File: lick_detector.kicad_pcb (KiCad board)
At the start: 2 copper layers, 20 x 20 mm, 16 parts, among them P1 CONN_FFC_8_VERT, P2 RECEPTACLE_2MM, U1 ADXL313, U2 BUFFER_TRI_STATE, U3 BUFFER_2_ELEMENT

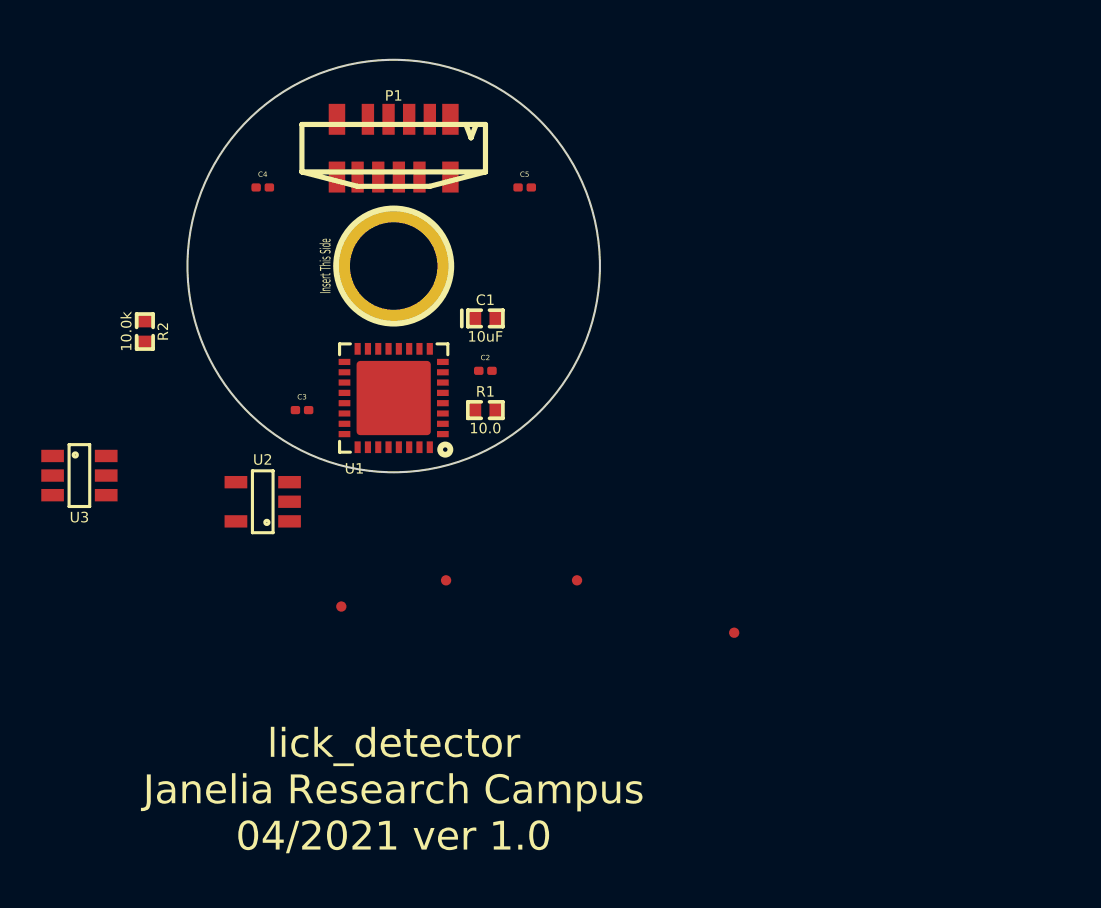
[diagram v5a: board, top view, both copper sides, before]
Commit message: Rearrange pcb footprints
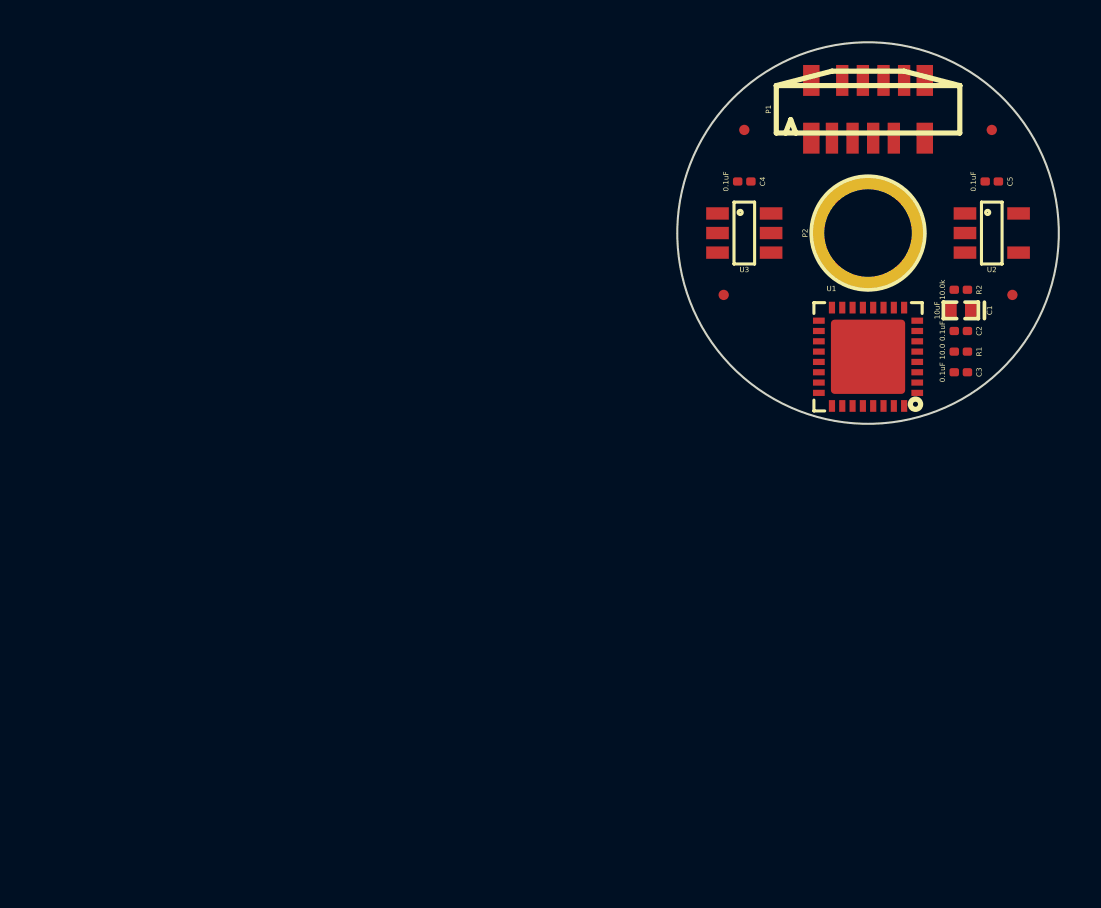
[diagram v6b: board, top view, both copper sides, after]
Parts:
- C2, C3, C4, C5: footprint lick_detector:C_0201_0603Metric -> lick_detector:SM0201
- R1, R2: footprint lick_detector:SM0402 -> lick_detector:SM0201
- moved R2 39.6 mm to (154.5, 102.8), turned to 180 degrees
- moved U2 37.7 mm to (156.0, 100.0), turned to 0 degrees
- moved U3 34.3 mm to (144.0, 100.0)
- moved C3 32.0 mm to (154.5, 106.8), turned to 180 degrees
- moved FID2 27.4 mm to (156.0, 95.0)
- moved FID1 26.2 mm to (144.0, 95.0)
- moved FID3 25.2 mm to (157.0, 103.0)
- moved FID4 23.9 mm to (143.0, 103.0)
- moved C4 23.4 mm to (144.0, 97.5), turned to 180 degrees
- moved R1 23.2 mm to (154.5, 105.8), turned to 180 degrees
- moved C2 23.1 mm to (154.5, 104.8), turned to 180 degrees
- moved U1 23.1 mm to (150.0, 106.0)
- moved P1 23.1 mm to (150.0, 94.0), turned to 0 degrees
- moved C1 23.1 mm to (154.5, 103.8), turned to 270 degrees
- moved P2 23.1 mm to (150.0, 100.0)
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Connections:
- R1 pad 1: Net-(R1-Pad1) -> VAA
- R1 pad 2: VAA -> Net-(R1-Pad2)
- U1 pad 5: Net-(R1-Pad1) -> Net-(R1-Pad2)
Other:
- board size 20 x 20 mm -> 18.5 x 18.5 mm

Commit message: Layout experimentation
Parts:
- U2: value BUFFER_TRI_STATE -> BUFFER_TRI_STATE_SMALL; footprint lick_detector:SOT-23-5 -> lick_detector:MICROPAK2_6LEAD
- U3: value BUFFER_2_ELEMENT -> BUFFER_2_ELEMENT_SMALL; footprint lick_detector:SOT-23-6 -> lick_detector:SOT-563
- moved FID3 3.35 mm to (158.5, 100.0)
- moved FID4 3.16 mm to (144.0, 106.0)
- moved C4 1.00 mm to (144.0, 98.5)
- moved C5 1.00 mm to (156.0, 98.5)
- moved FID1 1.00 mm to (144.0, 94.0)
- moved FID2 1.00 mm to (156.0, 94.0)
- moved C1 0.25 mm to (154.8, 103.8)
- moved C2 0.25 mm to (154.8, 104.8)
- moved C3 0.25 mm to (154.8, 106.8)
- moved R1 0.25 mm to (154.8, 105.8)
- moved R2 0.25 mm to (154.8, 102.8)
- turned U2 to 270 degrees
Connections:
- P1 pad 2: (no net) -> /INT1
- P1 pad 3: (no net) -> /INT2
- P1 pad 4: (no net) -> /MISO
- P1 pad 5: (no net) -> /MOSI
- P1 pad 6: (no net) -> /~CS
- P1 pad 7: (no net) -> /SCK
- U1 pad 24: (no net) -> /MOSI
- U1 pad 26: (no net) -> /SCK
- U2 pad 4: (no net) -> /MISO
- U2 pad 5: VAA -> (no net)
- U3 pad 4: (no net) -> /INT2
- U3 pad 6: (no net) -> /INT1
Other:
- net class POWER: clearance 0.1016 -> 0.0762; trace_width 0.4064 -> 0.1524; via_dia 0.889 -> 0.4064; via_drill 0.635 -> 0.254
- net class SIGNAL added: clearance 0.0762, trace_width 0.1524, via_dia 0.4064, via_drill 0.254
- rule trace_min: 0.2 -> 0.1016
- rule via_min_drill: 0.3 -> 0.254
- rule via_min_size: 0.4 -> 0.4064

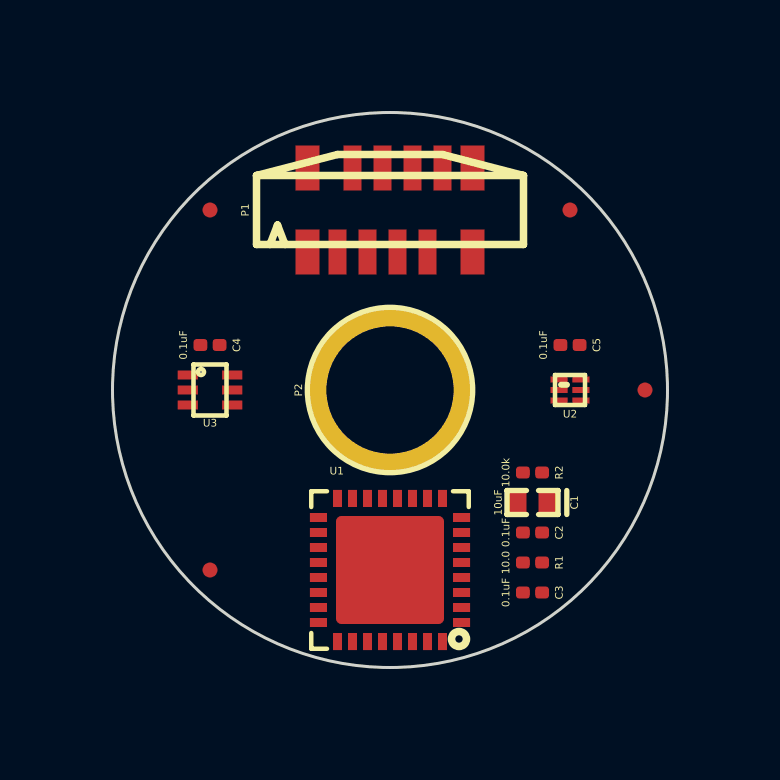
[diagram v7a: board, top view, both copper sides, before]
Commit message: Auto routed layout
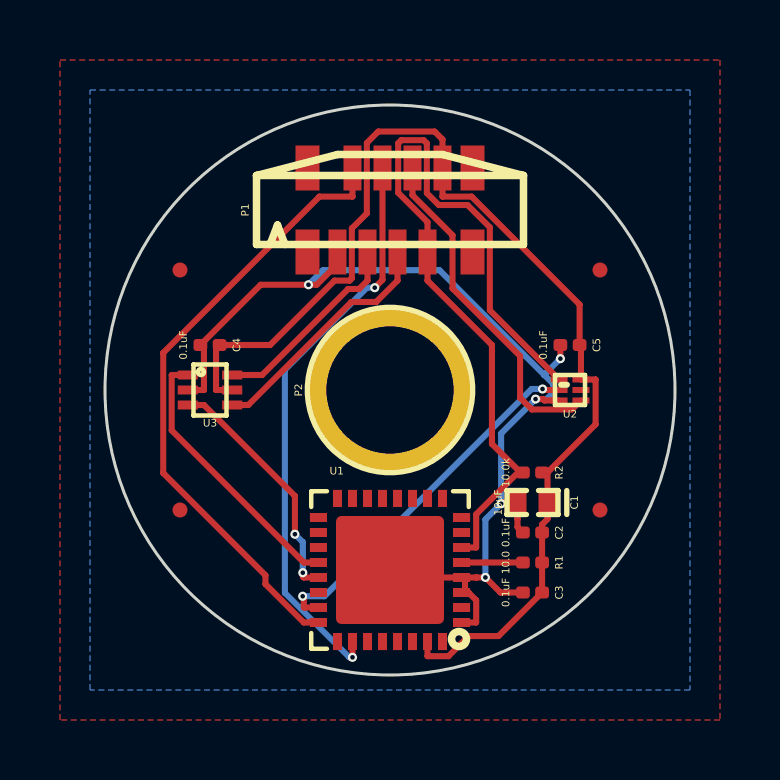
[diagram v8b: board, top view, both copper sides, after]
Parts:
- moved FID2 10.0 mm to (157.0, 104.0)
- moved FID3 4.27 mm to (157.0, 96.0)
- moved FID1 2.24 mm to (143.0, 96.0)
- moved FID4 2.24 mm to (143.0, 104.0)
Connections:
- P1 pad 2: /INT1 -> /MOSI
- P1 pad 3: /INT2 -> /INT1
- P1 pad 4: /MISO -> /SCK
- P1 pad 5: /MOSI -> /INT2
- P1 pad 6: /~CS -> /MISO
- P1 pad 7: /SCK -> /~CS
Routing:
- net VAA: track 0.00 -> 39.1 mm
- net GND: track 0.00 -> 36.4 mm, vias 0 -> 5
- net /~CS: track 0.00 -> 27.7 mm
- net /MOSI: track 0.00 -> 20.8 mm
- net /SCK: track 0.00 -> 19.3 mm, vias 0 -> 2
- net /MISO_UB: track 0.00 -> 12.3 mm, vias 0 -> 2
- net /MISO: track 0.00 -> 11.5 mm
- net /INT1_UB: track 0.00 -> 9.10 mm
- net /INT2: track 0.00 -> 8.18 mm
- net /INT2_UB: track 0.00 -> 8.16 mm, vias 0 -> 2
- net /INT1: track 0.00 -> 6.77 mm
- net Net-(R1-Pad2): track 0.00 -> 2.05 mm
- added copper zone on B.Cu, net GND
- added copper zone on F.Cu, net VAA
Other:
- board size 18.5 x 18.5 mm -> 19 x 19 mm
- net class Default: via_dia 0.6096 -> 0.3048; via_drill 0.3048 -> 0.1524
- net class POWER: via_dia 0.4064 -> 0.3048; via_drill 0.254 -> 0.1524
- net class SIGNAL: via_dia 0.4064 -> 0.3048; via_drill 0.254 -> 0.1524
- rule via_min_drill: 0.254 -> 0.1524
- rule via_min_size: 0.4064 -> 0.254
